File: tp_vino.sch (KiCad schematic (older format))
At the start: 0 parts

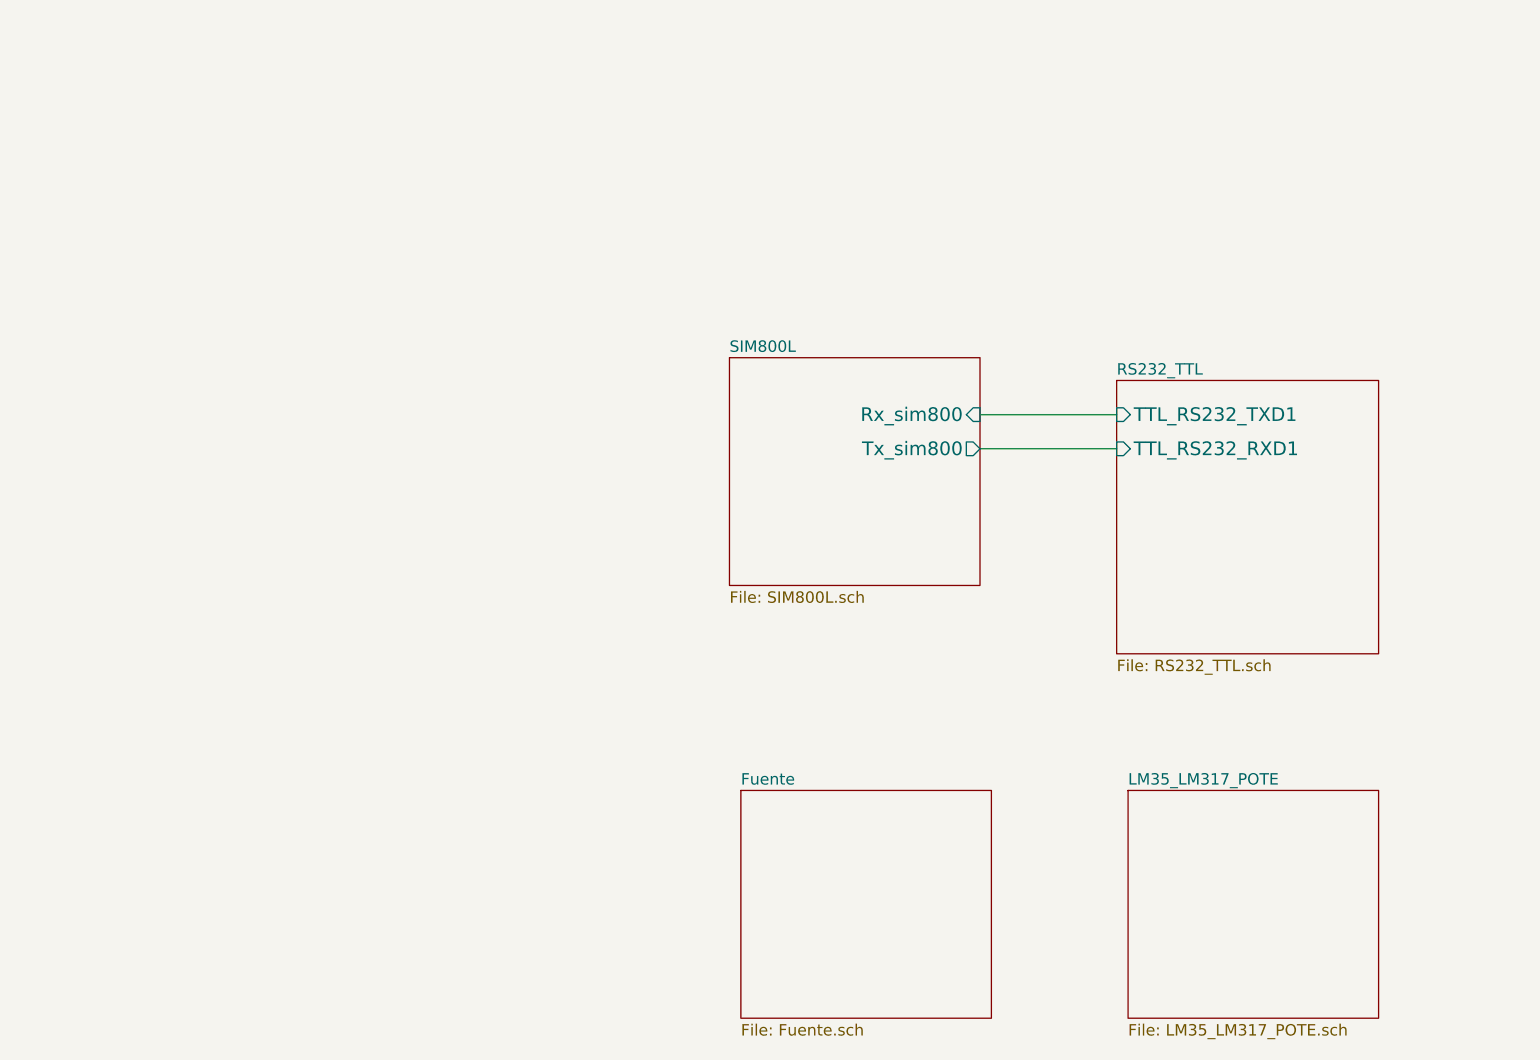
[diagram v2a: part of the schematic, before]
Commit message: Modificaciones en el schematic debida a los warning por powerflag y conectores mal definido como input en vez de pasive.
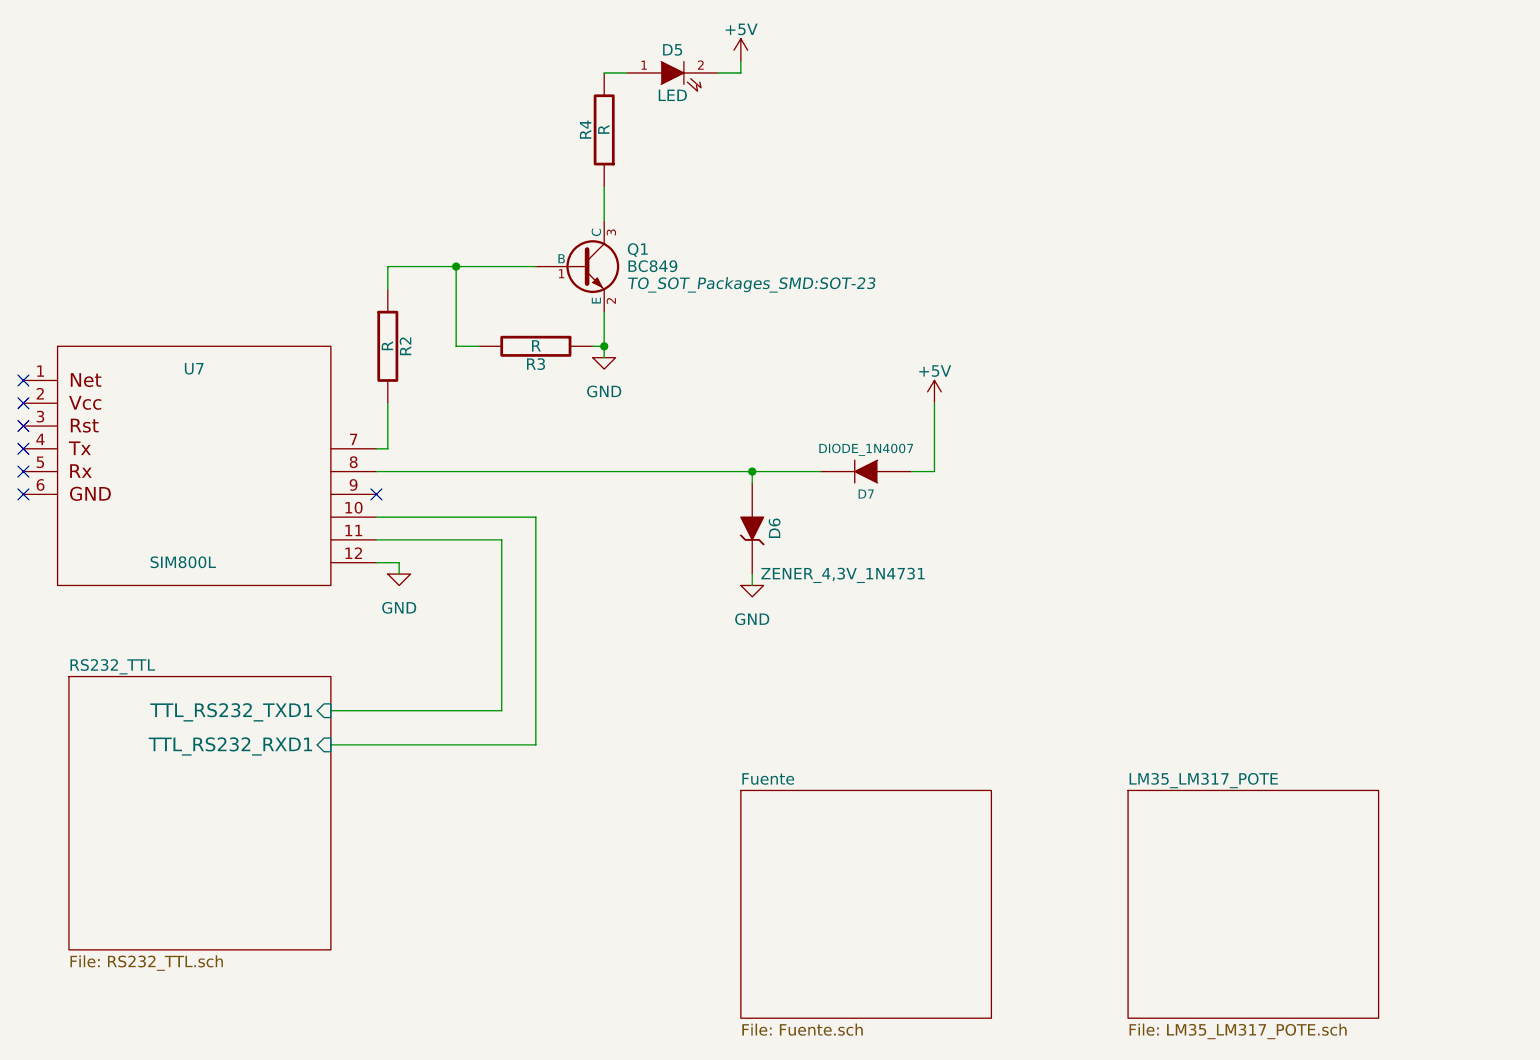
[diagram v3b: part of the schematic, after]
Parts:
- added D5: LED, LEDs:LED_1206, symbol LED
- added D6: ZENER_4,3V_1N4731, Diodes_SMD:SOD-123, symbol ZENER
- added D7: DIODE_1N4007, Diodes_SMD:SOD-123, symbol DIODE
- added Q1: BC849, TO_SOT_Packages_SMD:SOT-23, symbol BC849
- added R2, R3, R4: R, SMD_Packages:SMD-1206_Pol, symbol R
- added U7: SIM800L, symbol SIM800L
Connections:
- net RS232_TTL/TTL_RS232_RXD1: now also U7.10 (TX)
- net RS232_TTL/TTL_RS232_TXD1: now also U7.11 (RX)
- new net: Q1.1 (B), R2.1, R3.2
- new net: R2.2, U7.7 (NET)
- new net: Q1.3 (C), R4.1
- new net: D5.1 (A), R4.2
- new net: D6.1 (A), D7.2 (K), U7.8 (VCC)
- new net +5V: D5.2 (K), D7.1 (A)
- new net GND: D6.2 (K), Q1.2 (E), R3.1, U7.12 (GND)
- no-connect marks 0 -> 7
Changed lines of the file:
@@
 $Descr A4 11693 8268
 encoding utf-8
-Sheet 1 6
+Sheet 1 5
 Title "TP_PLACA_BASE_F_VINO"
 Date "2016-11-02"
@@
 $EndDescr
 $Sheet
-S 5550 2250 1150 1200
+S 950  3550 1150 1200
 U 581A0DA2
 F0 "RS232_TTL" 50
 F1 "RS232_TTL.sch" 50
-F2 "TTL_RS232_TXD1" I L 5550 2400 60
-F3 "TTL_RS232_RXD1" I L 5550 2550 60
+F2 "TTL_RS232_TXD1" I R 2100 3700 60
+F3 "TTL_RS232_RXD1" I R 2100 3850 60
 $EndSheet
 Text Notes 8550 2000 0    118  ~ 0
@@
 $EndSheet
 $Sheet
-S 3850 2150 1100 1000
-U 581A0DA4
-F0 "SIM800L" 50
-F1 "SIM800L.sch" 50
-F2 "Rx_sim800" I R 4950 2400 60
-F3 "Tx_sim800" O R 4950 2550 60
-$EndSheet
-$Sheet
 S 5600 4050 1100 1000
 U 581A0DA5
@@
 F1 "LM35_LM317_POTE.sch" 50
 $EndSheet
-Wire Wire Line
-	4950 2400 5550 2400
-Wire Wire Line
-	4950 2550 5550 2550
 $Sheet
 S 7500 3250 1100 1000
@@
 F1 "Buttons_Leds.sch" 50
 $EndSheet
+$Comp
+L GND #PWR01
+U 1 1 581C9EAC
+P 2400 3100
+F 0 "#PWR01" H 2400 2850 50  0001 C CNN
+F 1 "GND" H 2400 2950 50  0000 C CNN
+F 2 "" H 2400 3100 50  0000 C CNN
+F 3 "" H 2400 3100 50  0000 C CNN
+	1    2400 3100
+	1    0    0    -1
+$EndComp
+$Comp
+L R R2
+U 1 1 581C9EB4
+P 2350 2100
+F 0 "R2" V 2430 2100 50  0000 C CNN
+F 1 "R" V 2350 2100 50  0000 C CNN
+F 2 "SMD_Packages:SMD-1206_Pol" V 2280 2100 50  0001 C CNN
+F 3 "" H 2350 2100 50  0000 C CNN
+	1    2350 2100
+	1    0    0    -1
+$EndComp
+$Comp
+L R R3
+U 1 1 581C9EBB
+P 3000 2100
+F 0 "R3" V 3080 2100 50  0000 C CNN
+F 1 "R" V 3000 2100 50  0000 C CNN
+F 2 "SMD_Packages:SMD-1206_Pol" V 2930 2100 50  0001 C CNN
+F 3 "" H 3000 2100 50  0000 C CNN
+	1    3000 2100
+	0    1    1    0
+$EndComp
+$Comp
+L BC849 Q1
+U 1 1 581C9EC2
+P 3200 1750
+F 0 "Q1" H 3400 1825 50  0000 L CNN
+F 1 "BC849" H 3400 1750 50  0000 L CNN
+F 2 "TO_SOT_Packages_SMD:SOT-23" H 3400 1675 50  0000 L CIN
+F 3 "" H 3200 1750 50  0000 L CNN
+	1    3200 1750
+	1    0    0    -1
+$EndComp
+$Comp
+L GND #PWR02
+U 1 1 581C9EC9
+P 3300 2150
+F 0 "#PWR02" H 3300 1900 50  0001 C CNN
+F 1 "GND" H 3300 2000 50  0000 C CNN
+F 2 "" H 3300 2150 50  0000 C CNN
+F 3 "" H 3300 2150 50  0000 C CNN
+	1    3300 2150
+	1    0    0    -1
+$EndComp
+$Comp
+L R R4
+U 1 1 581C9ECF
+P 3300 1150
+F 0 "R4" V 3380 1150 50  0000 C CNN
+F 1 "R" V 3300 1150 50  0000 C CNN
+F 2 "SMD_Packages:SMD-1206_Pol" V 3230 1150 50  0001 C CNN
+F 3 "" H 3300 1150 50  0000 C CNN
+	1    3300 1150
+	-1   0    0    1
+$EndComp
+$Comp
+L LED D5
+U 1 1 581C9ED6
+P 3600 900
+F 0 "D5" H 3600 1000 50  0000 C CNN
+F 1 "LED" H 3600 800 50  0000 C CNN
+F 2 "LEDs:LED_1206" H 3600 900 50  0001 C CNN
+F 3 "" H 3600 900 50  0000 C CNN
+	1    3600 900
+	1    0    0    -1
+$EndComp
+NoConn ~ 750  2750
+NoConn ~ 750  2650
+NoConn ~ 750  2550
+NoConn ~ 750  2450
+$Comp
+L +5V #PWR03
+U 1 1 581C9EE3
+P 3900 850
+F 0 "#PWR03" H 3900 700 50  0001 C CNN
+F 1 "+5V" H 3900 990 50  0000 C CNN
+F 2 "" H 3900 850 50  0000 C CNN
+F 3 "" H 3900 850 50  0000 C CNN
+	1    3900 850
+	1    0    0    -1
+$EndComp
+$Comp
+L ZENER D6
+U 1 1 581C9EE9
+P 3950 2900
+F 0 "D6" H 3950 3000 50  0000 C CNN
+F 1 "ZENER_4,3V_1N4731" V 4150 3300 50  0000 C CNN
+F 2 "Diodes_SMD:SOD-123" H 3950 2900 50  0001 C CNN
+F 3 "" H 3950 2900 50  0000 C CNN
+	1    3950 2900
+	0    1    1    0
+$EndComp
+$Comp
+L GND #PWR04
+U 1 1 581C9EF0
+P 3950 3150
+F 0 "#PWR04" H 3950 2900 50  0001 C CNN
+F 1 "GND" H 3950 3000 50  0000 C CNN
+F 2 "" H 3950 3150 50  0000 C CNN
+F 3 "" H 3950 3150 50  0000 C CNN
+	1    3950 3150
+	1    0    0    -1
+$EndComp
+$Comp
+L DIODE D7
+U 1 1 581C9EF6
+P 4450 2650
+F 0 "D7" H 4450 2750 40  0000 C CNN
+F 1 "DIODE_1N4007" H 4450 2550 40  0000 C CNN
+F 2 "Diodes_SMD:SOD-123" H 4450 2650 60  0001 C CNN
+F 3 "" H 4450 2650 60  0000 C CNN
+	1    4450 2650
+	-1   0    0    1
+$EndComp
+$Comp
+L +5V #PWR05
+U 1 1 581C9EFD
+P 4750 2350
+F 0 "#PWR05" H 4750 2200 50  0001 C CNN
+F 1 "+5V" H 4750 2490 50  0000 C CNN
+F 2 "" H 4750 2350 50  0000 C CNN
+F 3 "" H 4750 2350 50  0000 C CNN
+	1    4750 2350
+	1    0    0    -1
+$EndComp
+NoConn ~ 2300 2750
+Wire Wire Line
+	2300 3050 2400 3050
+Wire Wire Line
+	2400 3050 2400 3100
+Wire Wire Line
+	2300 2950 2850 2950
+Wire Wire Line
+	2300 2850 3000 2850
+Wire Wire Line
+	3300 1950 3300 2150
+Connection ~ 3300 2100
+Wire Wire Line
+	2350 1750 3000 1750
+Wire Wire Line
+	3300 1400 3300 1550
+Wire Wire Line
+	3800 900  3900 900
+Wire Wire Line
+	3900 900  3900 850
+Wire Wire Line
+	3950 2650 3950 2700
+Wire Wire Line
+	3950 3100 3950 3150
+Wire Wire Line
+	4750 2350 4750 2650
+Wire Wire Line
+	4750 2650 4650 2650
+Connection ~ 3950 2650
+Wire Wire Line
+	2350 1850 2350 1750
+Wire Wire Line
+	2750 2100 2650 2100
+Wire Wire Line
+	2650 2100 2650 1750
+Connection ~ 2650 1750
+Wire Wire Line
+	3250 2100 3300 2100
+Wire Wire Line
+	3400 900  3300 900
+$Comp
+L SIM800L U7
+U 1 1 581C9F1C
+P 1600 2600
+F 0 "U7" H 1500 3000 50  0000 C CNN
+F 1 "SIM800L" H 1450 2150 50  0000 C CNN
+F 2 "" H 950 2650 50  0000 C CNN
+F 3 "" H 950 2650 50  0000 C CNN
+	1    1600 2600
+	1    0    0    -1
+$EndComp
+Wire Wire Line
+	2100 3700 2850 3700
+Wire Wire Line
+	2850 3700 2850 2950
+Wire Wire Line
+	3000 2850 3000 3850
+Wire Wire Line
+	3000 3850 2100 3850
+Wire Wire Line
+	2300 2550 2350 2550
+Wire Wire Line
+	2350 2550 2350 2350
+Wire Wire Line
+	2300 2650 4250 2650
+NoConn ~ 750  2250
+NoConn ~ 750  2350
 $EndSCHEMATC

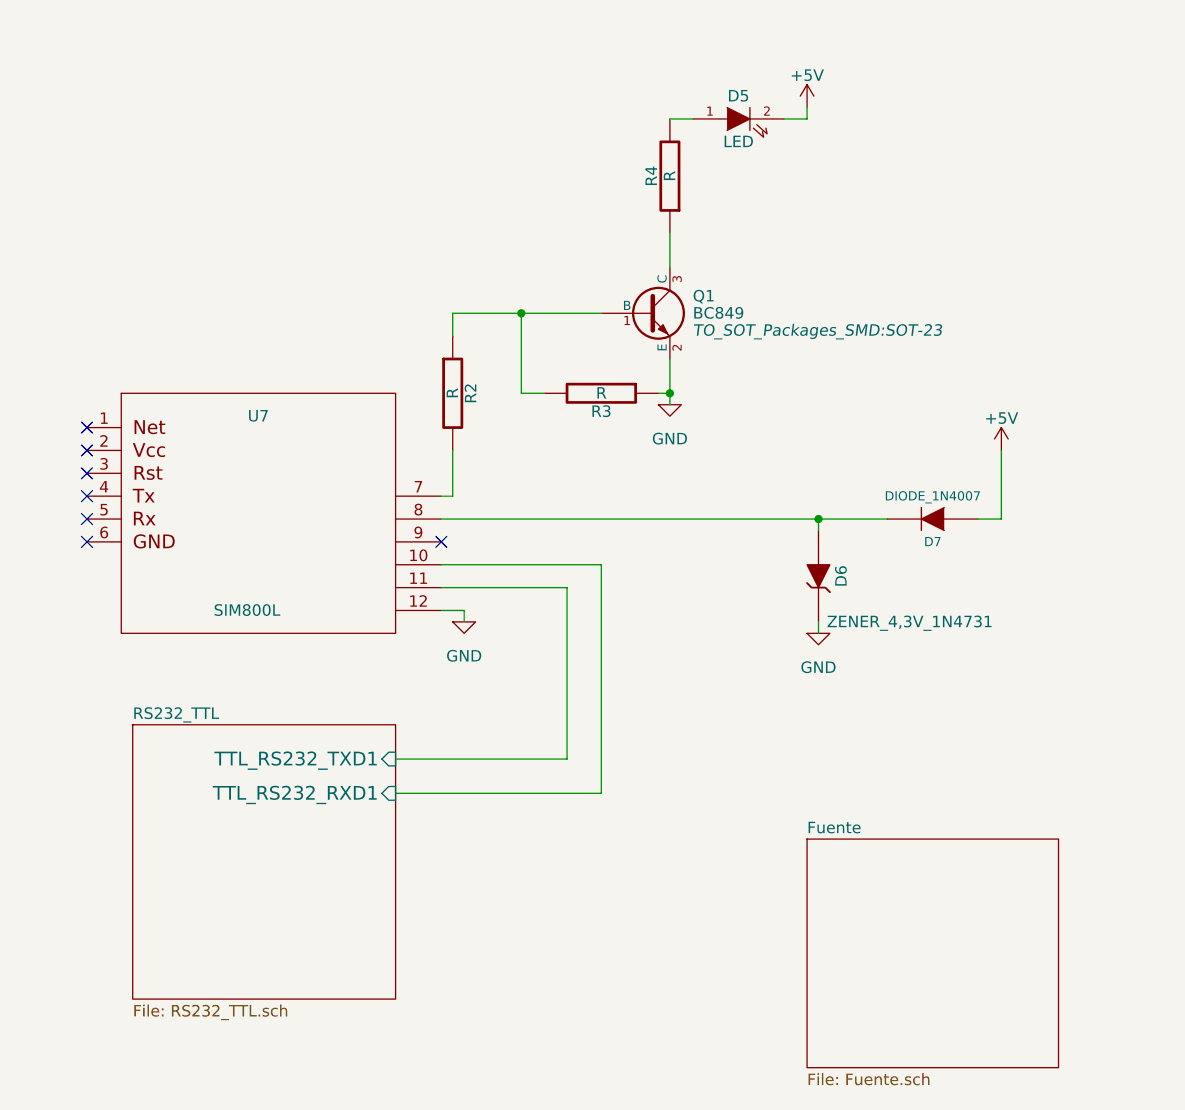
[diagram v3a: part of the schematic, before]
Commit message: Modificaciones en el schematic dado los componentes comprados empiezo a ordenar los componentes en una dimension estimada de 10x6 cm.
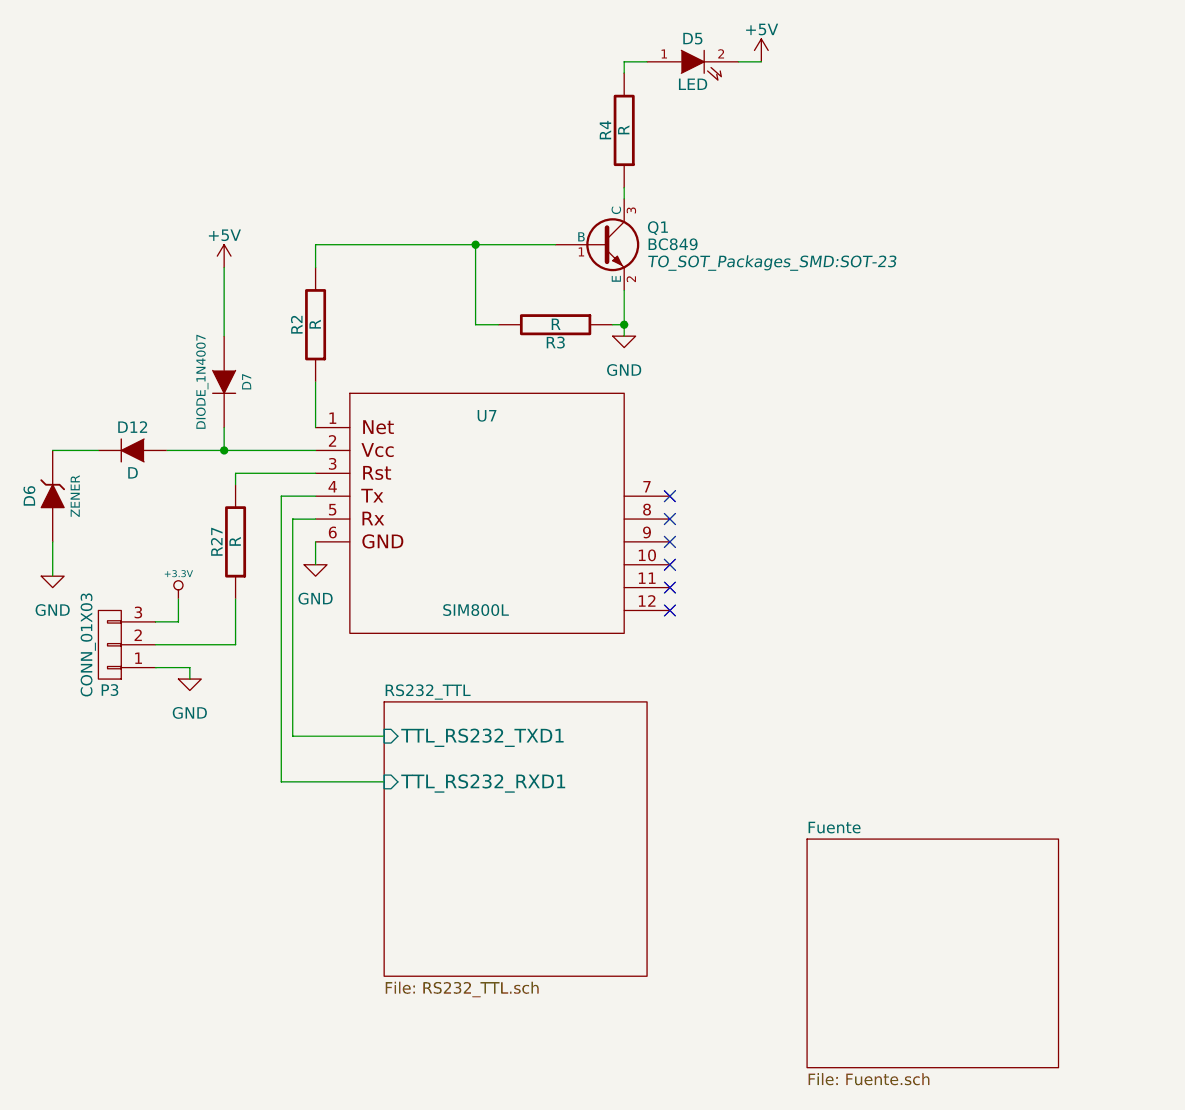
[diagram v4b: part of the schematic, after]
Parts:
- added D12: D, Diodes_SMD:MELF_Handsoldering, symbol D
- added P3: CONN_01X03, Pin_Headers:Pin_Header_Straight_1x03, symbol CONN_01X03
- added R27: R, SMD_Packages:SMD-1206_Pol, symbol R
- D5: footprint LEDs:LED_1206 -> Diodes_SMD:MELF_Handsoldering
- D6: value ZENER_4,3V_1N4731 -> ZENER; footprint Diodes_SMD:SOD-123 -> Diodes_SMD:MELF_Handsoldering
- D7: footprint Diodes_SMD:SOD-123 -> Diodes_SMD:MELF_Handsoldering
- U7: footprint (none) -> sim800L_ok:sim
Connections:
- net GND: now also D6.1 (A), U7.6 (P6), P3.1 (P1); no longer D6.2 (K), U7.12 (GND)
- net RS232_TTL/TTL_RS232_RXD1: now also U7.4 (P4); no longer U7.10 (TX)
- net RS232_TTL/TTL_RS232_TXD1: now also U7.5 (P5); no longer U7.11 (RX)
- net at Q1.1 (B), R3.2: now also R2.2; no longer R2.1
- net at U7.7 (NET): no longer R2.2
- net at U7.1 (P1): now also R2.1
- net at U7.2 (P2): now also D7.2 (K), D12.2 (A)
- net at U7.3 (P3): now also R27.2
- new net: P3.2 (P2), R27.1
- new net: D12.1 (K), D6.2 (K)
- new net +3.3V: P3.3 (P3)
- now unconnected: U7.8 (VCC)
- no-connect marks 7 -> 6
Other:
- moved on the sheet: D5, D7, Q1, R2, R3, R4, U7

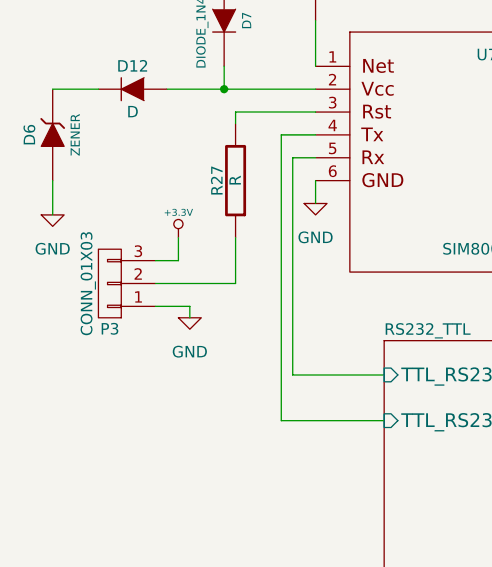
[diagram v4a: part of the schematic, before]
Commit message: Ruteo del PCB, agrego una salida de 5v y 3v en el esquematico
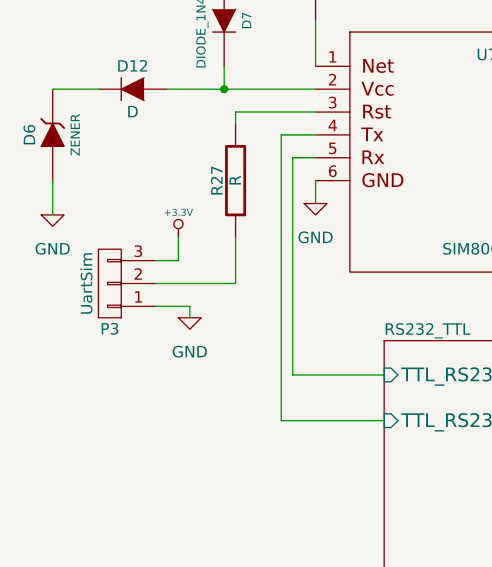
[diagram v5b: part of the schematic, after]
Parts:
- P3: value CONN_01X03 -> UartSim
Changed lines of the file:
@@
 P 850 3200
 F 0 "P3" H 850 3400 50  0000 C CNN
-F 1 "CONN_01X03" V 950 3200 50  0000 C CNN
+F 1 "UartSim" V 950 3200 50  0000 C CNN
 F 2 "Pin_Headers:Pin_Header_Straight_1x03" H 850 3200 50  0001 C CNN
 F 3 "" H 850 3200 50  0000 C CNN

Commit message: Agrego los graficos para el esquematico en 3d.
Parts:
- D12, D6, D7: footprint Diodes_SMD:MELF_Handsoldering -> Diodes_SMD:MELF_Standard
- D5: footprint Diodes_SMD:MELF_Handsoldering -> SMD_Packages:SMD-1206_Pol
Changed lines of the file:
@@
 F 0 "D5" H 3400 750 50  0000 C CNN
 F 1 "LED" H 3400 550 50  0000 C CNN
-F 2 "Diodes_SMD:MELF_Handsoldering" H 3400 650 50  0001 C CNN
+F 2 "SMD_Packages:SMD-1206_Pol" H 3400 650 50  0001 C CNN
 F 3 "" H 3400 650 50  0000 C CNN
 	1    3400 650
@@
 F 0 "D7" H 1350 2150 40  0000 C CNN
 F 1 "DIODE_1N4007" H 1350 1950 40  0000 C CNN
-F 2 "Diodes_SMD:MELF_Handsoldering" H 1350 2050 60  0001 C CNN
+F 2 "Diodes_SMD:MELF_Standard" H 1350 2050 60  0001 C CNN
 F 3 "" H 1350 2050 60  0000 C CNN
 	1    1350 2050
@@
 F 0 "D12" H 950 2450 50  0000 C CNN
 F 1 "D" H 950 2250 50  0000 C CNN
-F 2 "Diodes_SMD:MELF_Handsoldering" H 950 2350 50  0001 C CNN
+F 2 "Diodes_SMD:MELF_Standard" H 950 2350 50  0001 C CNN
 F 3 "" H 950 2350 50  0000 C CNN
 	1    950  2350
@@
 F 0 "D6" H 600 2650 50  0000 C CNN
 F 1 "ZENER" H 600 2450 40  0000 C CNN
-F 2 "Diodes_SMD:MELF_Handsoldering" H 600 2550 60  0001 C CNN
+F 2 "Diodes_SMD:MELF_Standard" H 600 2550 60  0001 C CNN
 F 3 "" H 600 2550 60  0000 C CNN
 	1    600  2550
